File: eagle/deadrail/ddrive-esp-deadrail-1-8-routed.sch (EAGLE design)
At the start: 20 parts, among them Q1 BSS123, Q2 BSS123, Q3 BSS123, Q4 BSS123

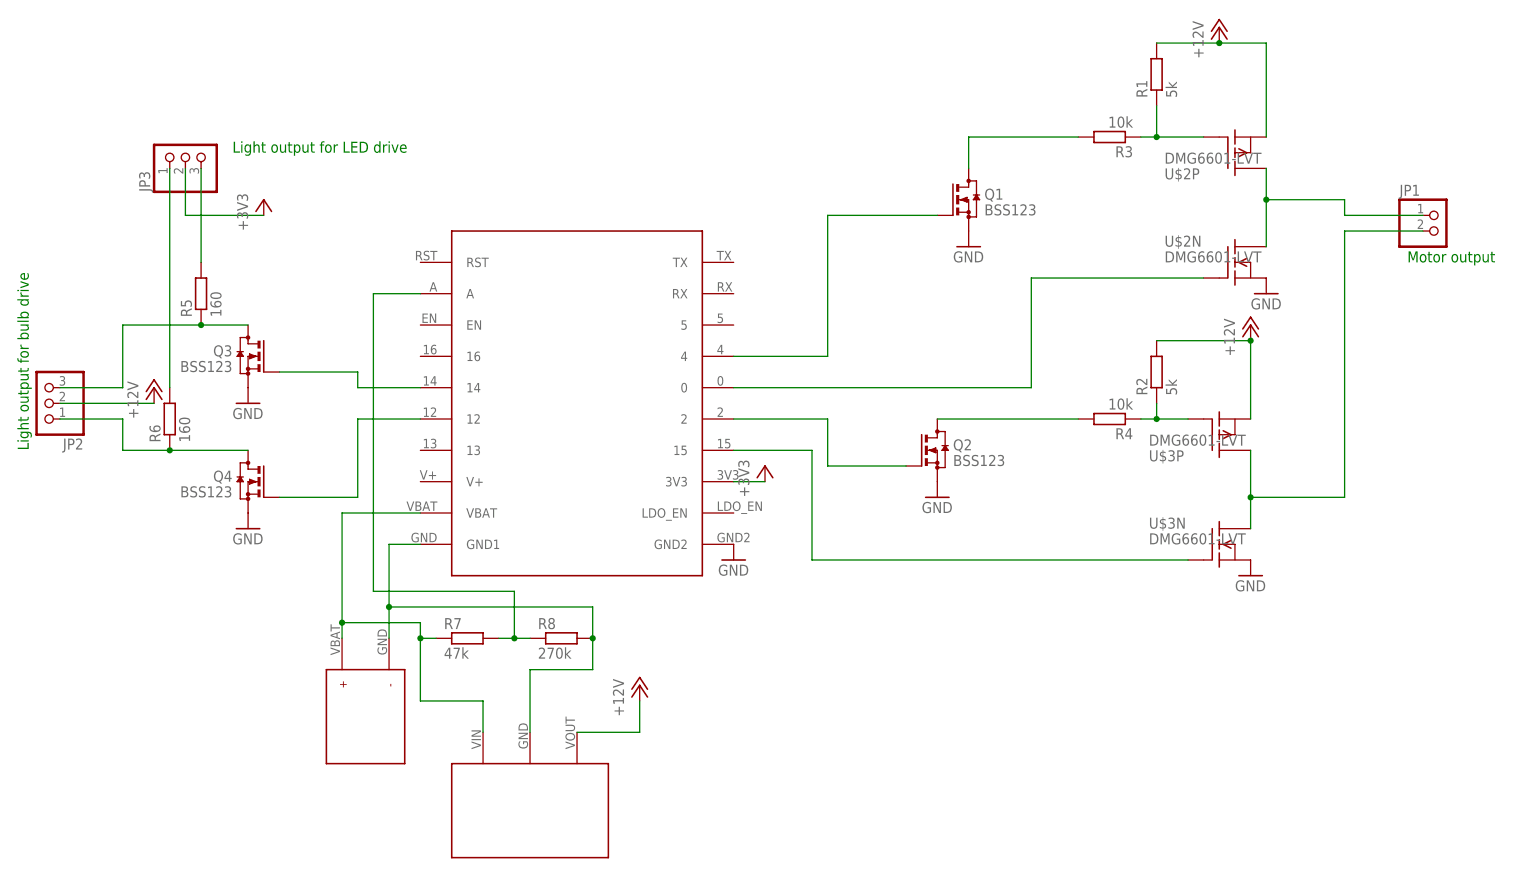
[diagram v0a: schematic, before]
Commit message: Adds all intermediate and the final schematic and board layout for the huzzah baseboard for esp-12 train decoder.
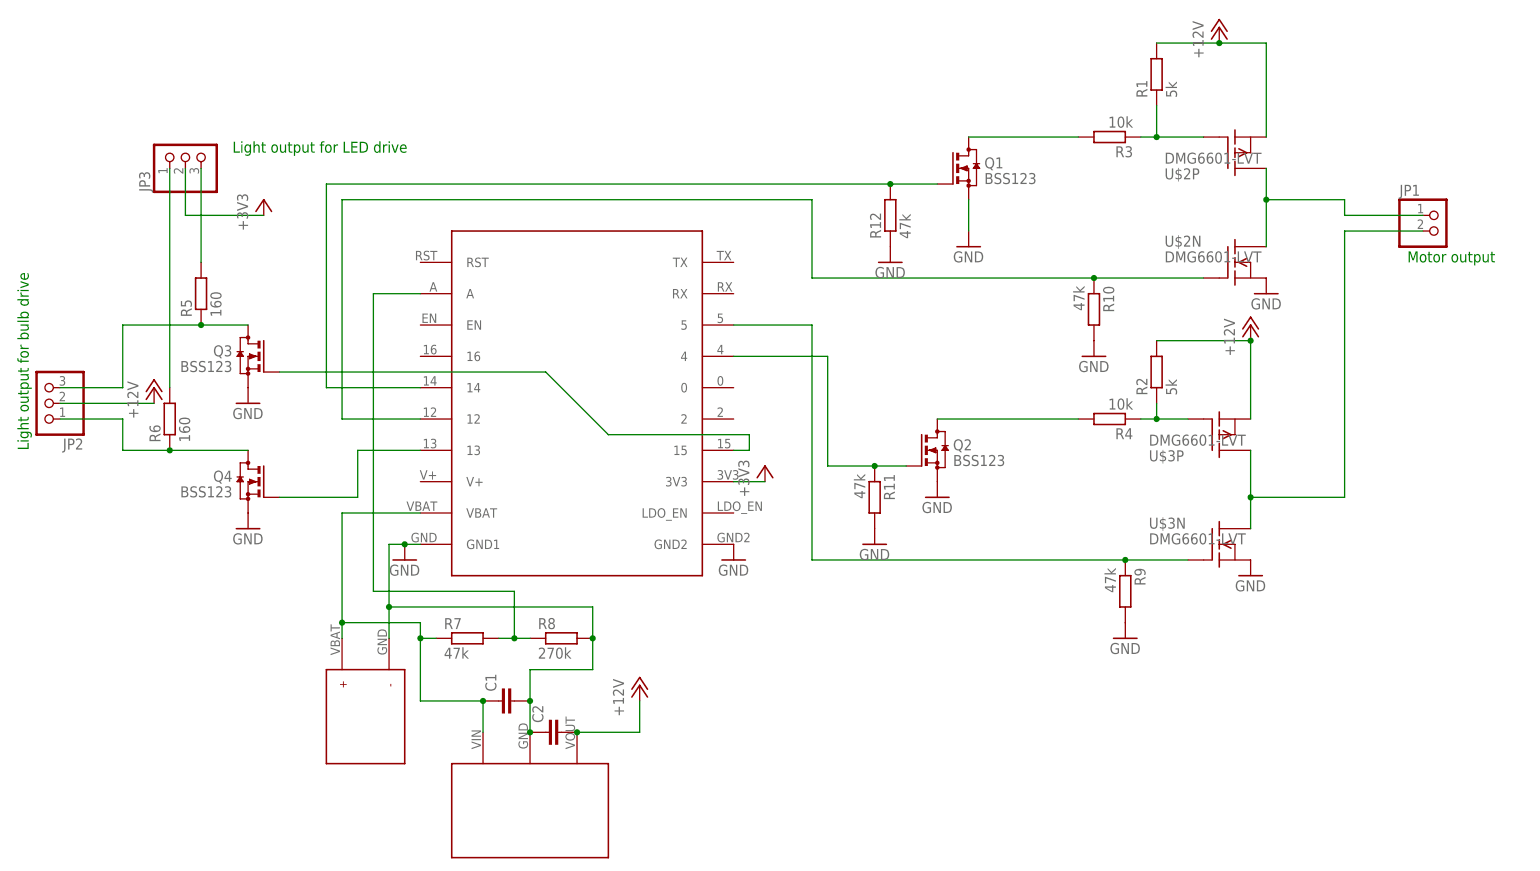
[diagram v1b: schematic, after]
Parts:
- added C1, C2: (no value), rcl:C-EUC1210
- added R10, R11, R12, R9: 47k, rcl:R-EU_R0805
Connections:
- removed net GND1: R8.2, U$1.GND1, U$4.P$1, U$5.GND
- net +12V: now also C2.2
- net GND: now also C1.2, C2.1, R10.2, R11.2, R12.1, R8.2, R9.2, U$1.GND1, U$4.P$1, U$5.GND
- net N$10: now also R9.1, U$1.5; no longer U$1.15
- net N$11: now also U$1.15; no longer U$1.14
- net N$12: now also U$1.13; no longer U$1.12
- net N$5: now also R12.2, U$1.14; no longer U$1.4
- net N$8: now also R10.1, U$1.12; no longer U$1.0
- net N$9: now also R11.1, U$1.4; no longer U$1.2
- net VBAT: now also C1.1
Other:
- moved on the sheet: Q1
